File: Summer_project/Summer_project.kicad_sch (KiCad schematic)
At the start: 7 parts, among them J1 USB_C_Receptacle_PowerOnly_6P, SW1 SW_Push

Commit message: change Clim to 1k from 330
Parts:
- R1: value 330 -> 1k
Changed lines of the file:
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@@
 			)
 		)
-		(property "Value" "330"
+		(property "Value" "1k"
 			(at 97.79 43.18 90)
 			(show_name no)

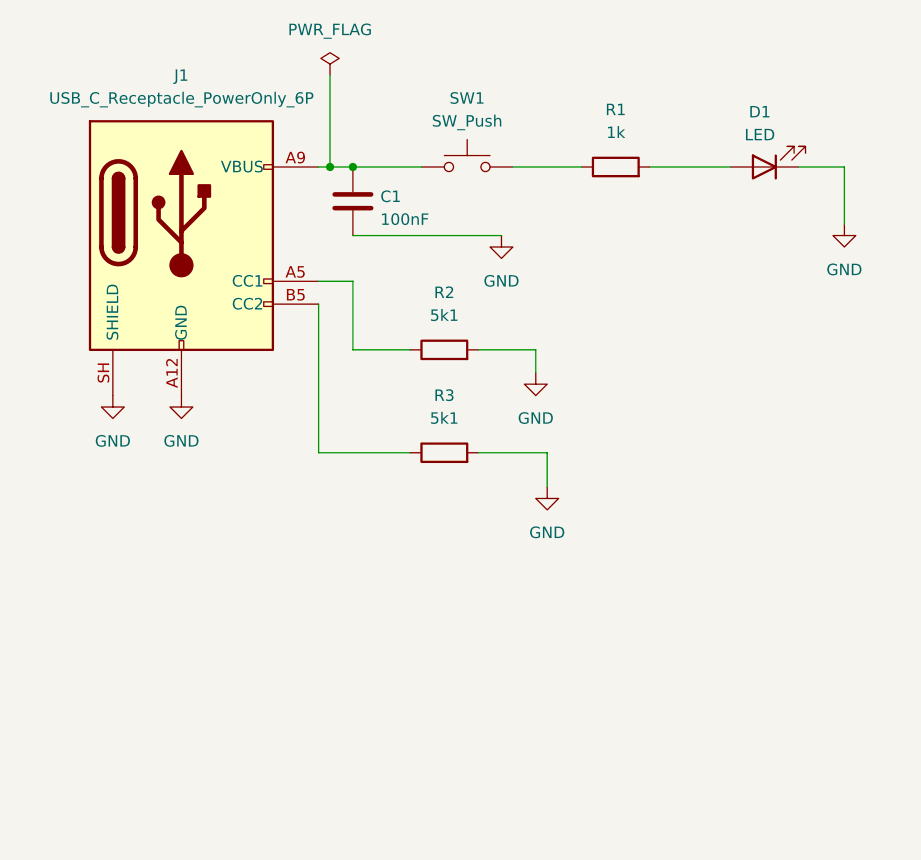
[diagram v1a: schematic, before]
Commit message: RSC_logo_with_3_LED
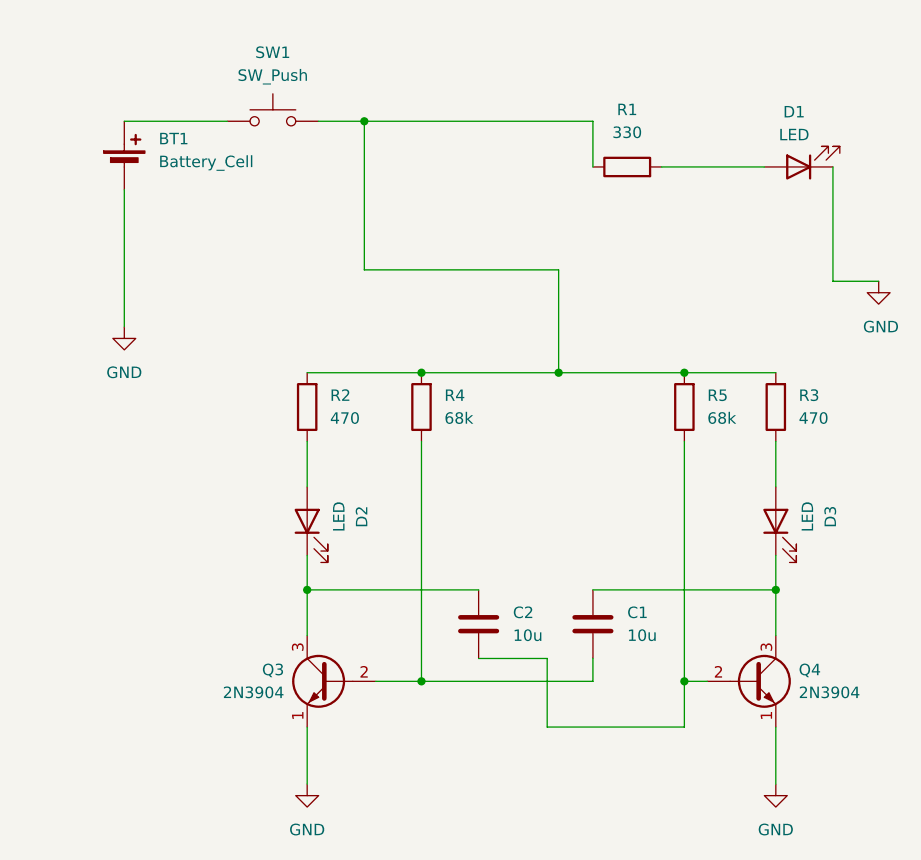
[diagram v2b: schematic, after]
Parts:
- removed J1: USB_C_Receptacle_PowerOnly_6P, symbol Connector:USB_C_Receptacle_PowerOnly_6P
- added BT1: Battery_Cell, Summer_project:BAT_BAT-HLD-005-THM, symbol Device:Battery_Cell
- added C2: 10u, Capacitor_THT:CP_Radial_D5.0mm_P2.00mm, symbol Device:C
- added D2, D3: LED, LED_THT:LED_D5.0mm, symbol Device:LED
- added Q3, Q4: 2N3904, Package_TO_SOT_THT:TO-92_Inline, symbol Transistor_BJT:2N3904
- added R4, R5: 68k, Resistor_THT:R_Axial_DIN0207_L6.3mm_D2.5mm_P7.62mm_Horizontal, symbol Device:R
- C1: value 100nF -> 10u; footprint (none) -> Capacitor_THT:CP_Radial_D5.0mm_P2.00mm
- D1: footprint (none) -> LED_THT:LED_D5.0mm
- R1: value 1k -> 330; footprint (none) -> Resistor_THT:R_Axial_DIN0207_L6.3mm_D2.5mm_P7.62mm_Horizontal
- R2, R3: value 5k1 -> 470; footprint (none) -> Resistor_THT:R_Axial_DIN0207_L6.3mm_D2.5mm_P7.62mm_Horizontal
- SW1: footprint (none) -> Button_Switch_THT:SW_PUSH_6mm
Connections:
- net GND: now also BT1.2 (-), Q3.1 (E), Q4.1 (E); no longer C1.2, R2.2, R3.2
- net at R1.1, SW1.2: now also R2.2, R3.2, R4.2, R5.2
- net at C1.1: now also D3.1 (K), Q4.3 (C); no longer SW1.1
- net at R2.1: now also D2.2 (A)
- net at R3.1: now also D3.2 (A)
- new net: C1.2, Q3.2 (B), R4.1
- new net: C2.2, Q4.2 (B), R5.1
- new net: C2.1, D2.1 (K), Q3.3 (C)
- new net: BT1.1 (+), SW1.1
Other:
- moved on the sheet: D1, R1, SW1
